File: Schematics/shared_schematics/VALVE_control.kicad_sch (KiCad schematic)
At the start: 4 parts, among them Q1 AO3400A

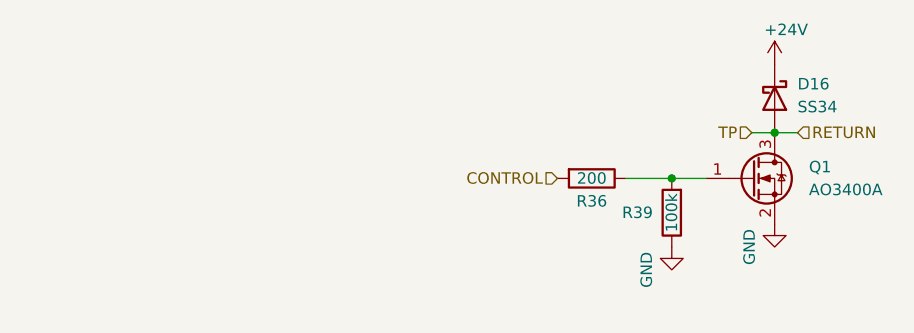
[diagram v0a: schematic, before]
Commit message: add decoupling, revise power circuitry (ferrite bead, LDO swap), merge shared-schemtic branch changes.
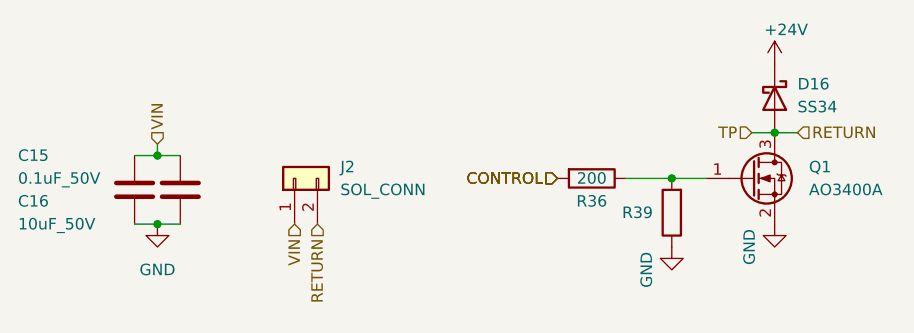
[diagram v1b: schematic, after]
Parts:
- added C15: 0.1uF_50V, Capacitor_SMD:C_0603_1608Metric, symbol Device:C
- added C16: 10uF_50V, Capacitor_SMD:C_1206_3216Metric, symbol Device:C
- added J2: SOL_CONN, CONNS:CONN02_530470260_MOL, symbol Connector_Generic:Conn_01x02
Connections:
- net GND: now also C15.2, C16.2
- net RETURN: now also J2.2 (Pin_2)
- new net VIN: C15.1, C16.1, J2.1 (Pin_1)
